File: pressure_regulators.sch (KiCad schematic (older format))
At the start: 18 parts, among them J10 CONN_01X04, J11 CONN_01X04, J9 CONN_01X04, U8 OpAmp-TLV2374

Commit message: Flipped silkscreen of left-side pins of ESP32; updated to KiCad 5
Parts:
- C1: footprint Capacitors_SMD:C_0603_HandSoldering -> Capacitor_SMD:C_0603_1608Metric_Pad1.05x0.95mm_HandSolder; symbol CP1 -> Device:CP1
- J10, J11, J9: footprint Pin_Headers:Pin_Header_Straight_1x04_Pitch2.54mm -> Connector_PinSocket_2.54mm:PinSocket_1x04_P2.54mm_Vertical; symbol CONN_01X04 -> ufcs-rescue:CONN_01X04
- R10, R11, R12, R13, R14, R15, R16, R17, R5, R6, R7, R8, R9: footprint Resistors_SMD:R_0603_HandSoldering -> Resistor_SMD:R_0603_1608Metric_Pad1.05x0.95mm_HandSolder; symbol R -> Device:R
- U8: footprint Housings_SOIC:SOIC-14_3.9x8.7mm_Pitch1.27mm -> Package_SO:SOIC-14_3.9x8.7mm_P1.27mm; symbol OpAmp-TLV2374 -> OpAmps-BJH:OpAmp-TLV2374

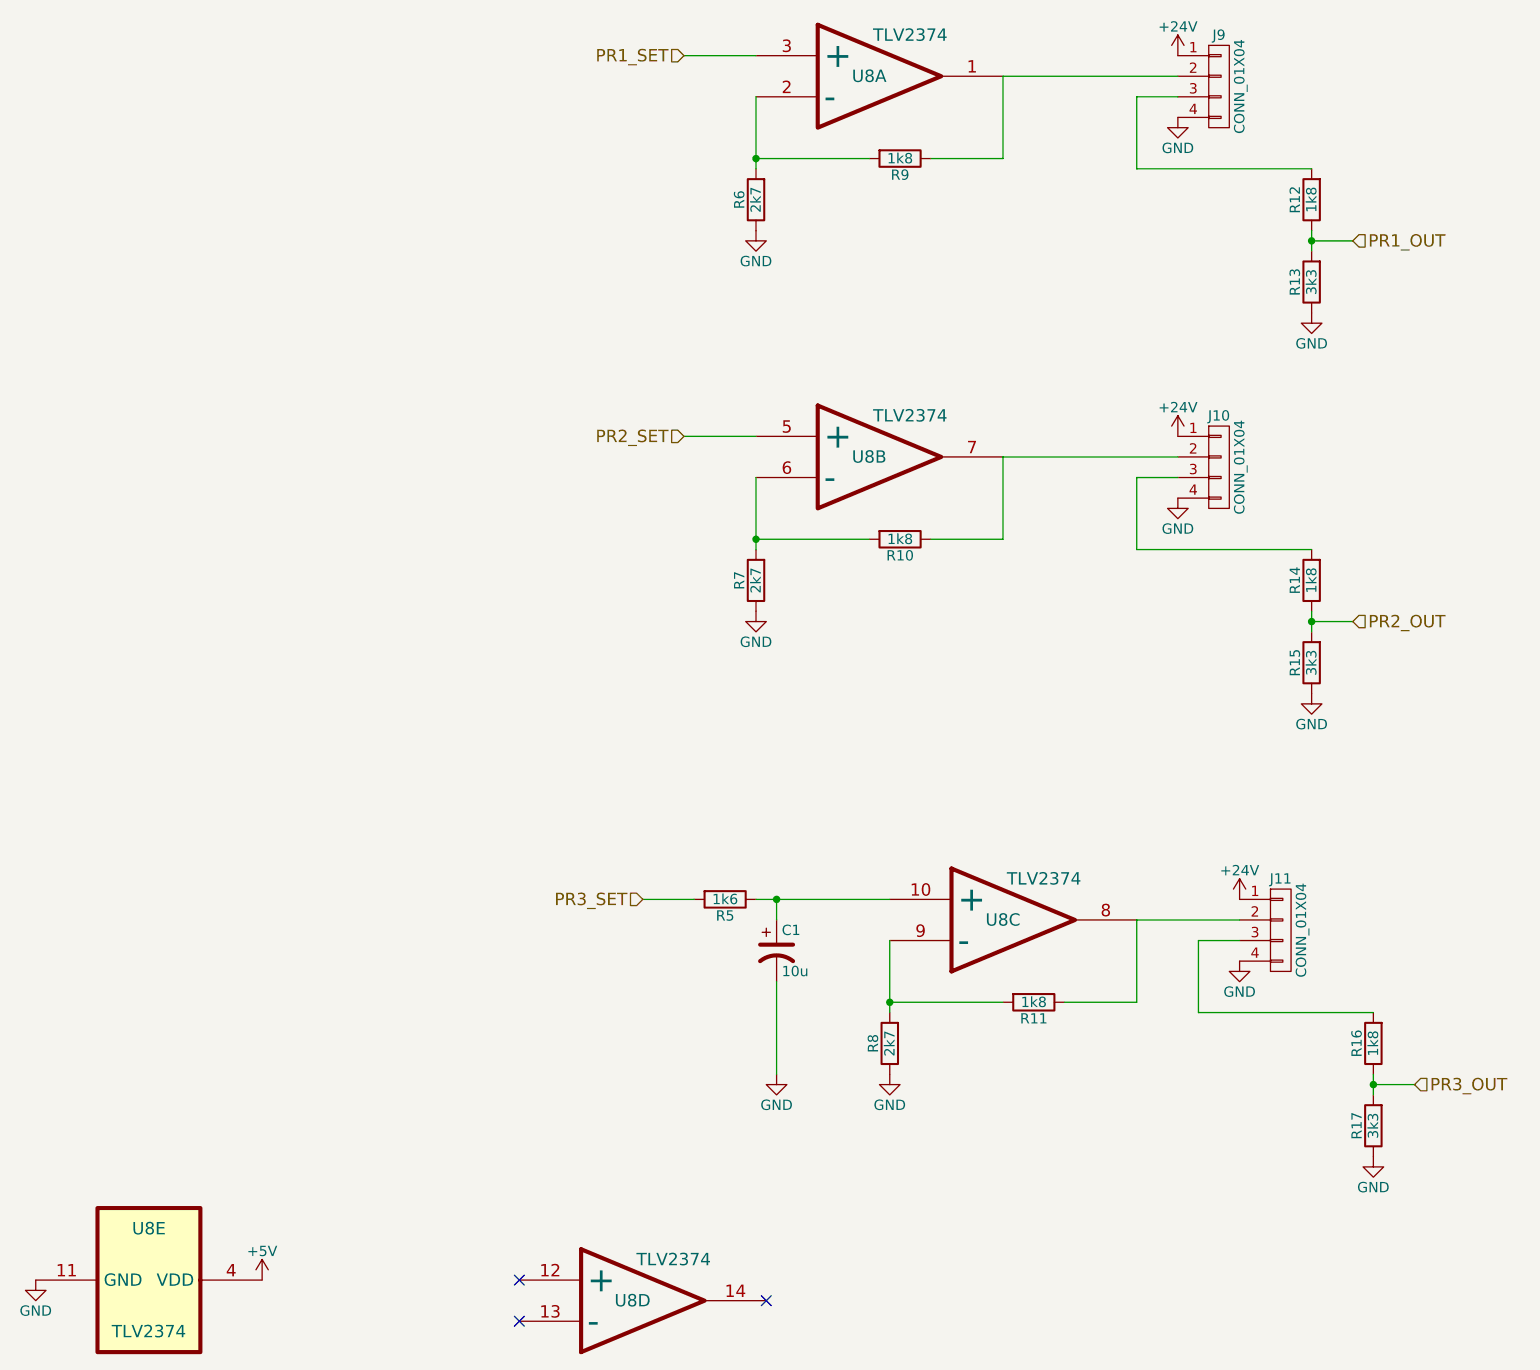
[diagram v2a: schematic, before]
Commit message: Add digital pressure reg connector; re-index resistor references; misc updates
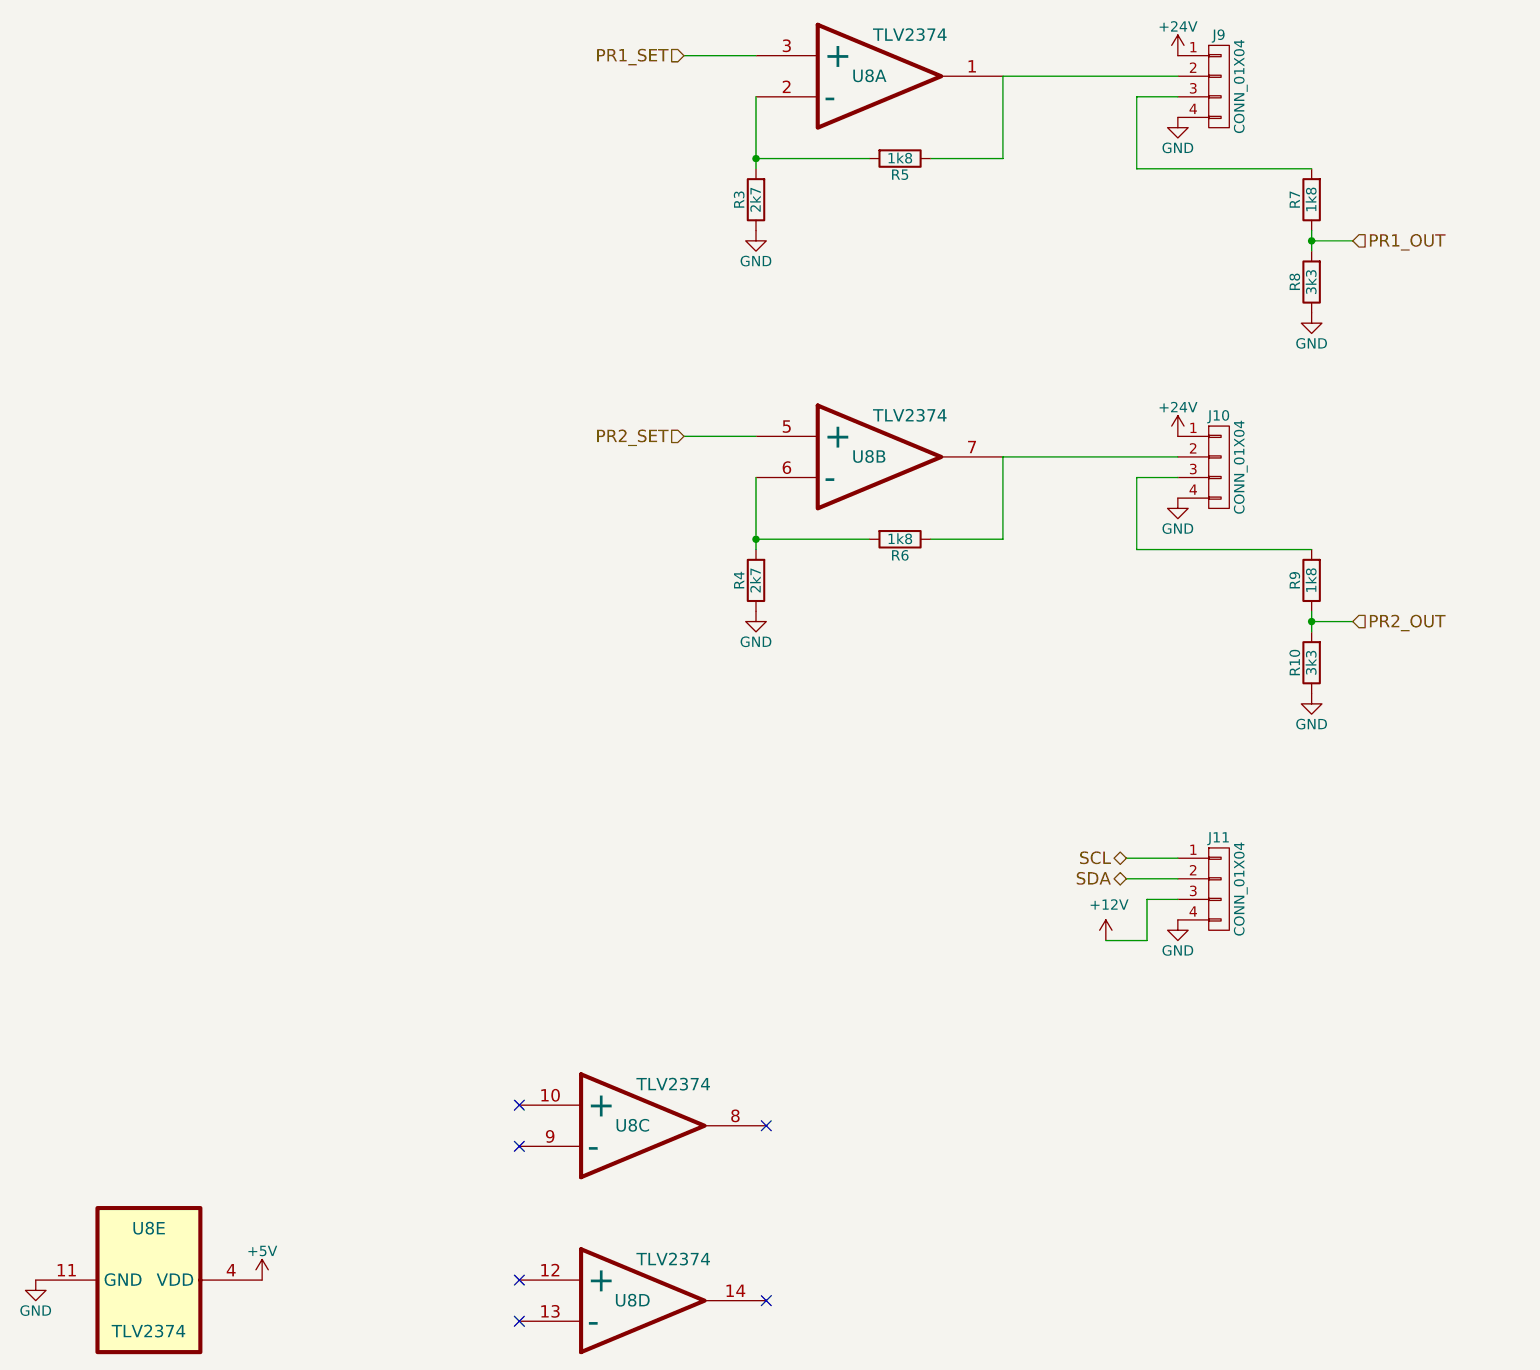
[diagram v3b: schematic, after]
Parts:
- removed C1: 10u, Capacitor_SMD:C_0603_1608Metric_Pad1.05x0.95mm_HandSolder, symbol Device:CP1
- removed R11, R16: 1k8, Resistor_SMD:R_0603_1608Metric_Pad1.05x0.95mm_HandSolder, symbol Device:R
- removed R17: 3k3, Resistor_SMD:R_0603_1608Metric_Pad1.05x0.95mm_HandSolder, symbol Device:R
- removed R5: 1k6, Resistor_SMD:R_0603_1608Metric_Pad1.05x0.95mm_HandSolder, symbol Device:R
- removed R8: 2k7, Resistor_SMD:R_0603_1608Metric_Pad1.05x0.95mm_HandSolder, symbol Device:R
- renumbered R15 to R10, R6 to R3, R7 to R4, R9 to R5, R10 to R6, R12 to R7, R13 to R8, R14 to R9
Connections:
- net +24V: no longer J11.1 (P1)
- net at U8.8: no longer J11.2 (P2)
- net +12V: now reaches J11.3 (P3)
- new net SCL: J11.1 (P1)
- new net SDA: J11.2 (P2)
- no-connect marks 3 -> 6
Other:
- moved on the sheet: U8C
